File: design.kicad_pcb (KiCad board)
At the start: 4 copper layers, 65 x 36 mm, 32 parts, among them J1 Conn_01x03

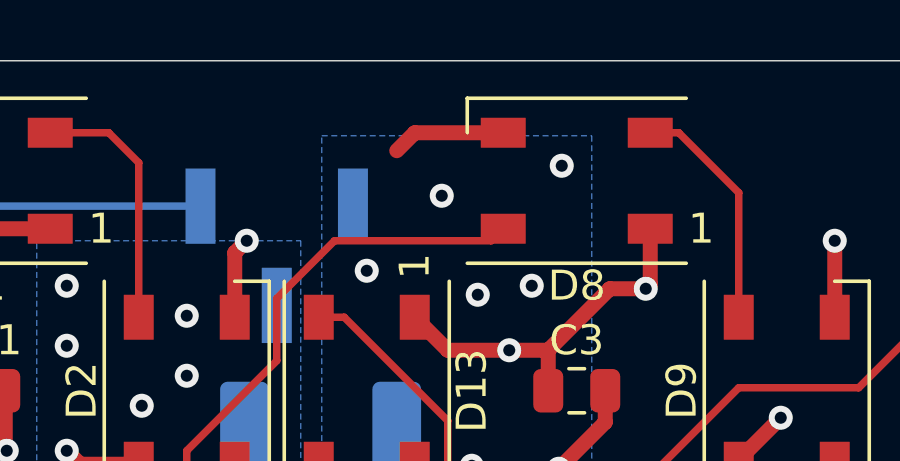
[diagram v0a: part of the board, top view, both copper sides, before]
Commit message: PCB: connect D8/3 to GND
Fix #1
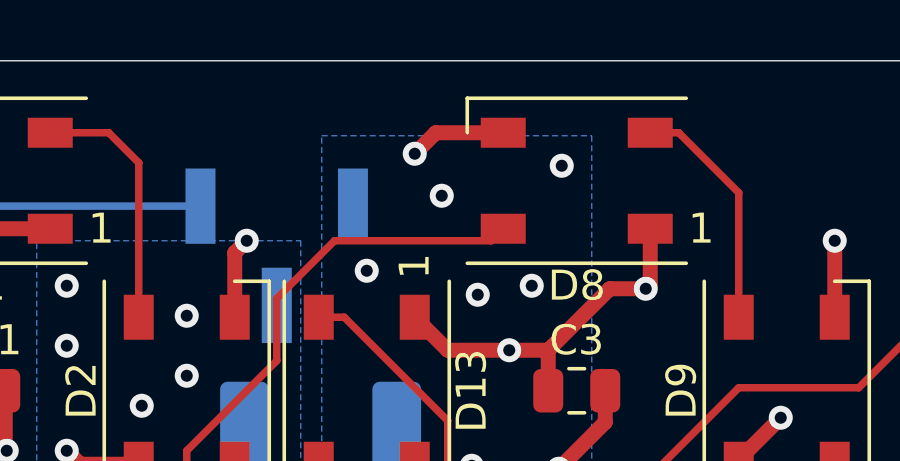
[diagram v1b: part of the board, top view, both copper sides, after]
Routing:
- net GND: track 77.9 -> 77.4 mm, vias 34 -> 35
